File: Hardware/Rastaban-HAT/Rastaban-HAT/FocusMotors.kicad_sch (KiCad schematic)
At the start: 9 parts, among them U6 TMC2208_SILENTSTEPSTICK, U7 DRV8838

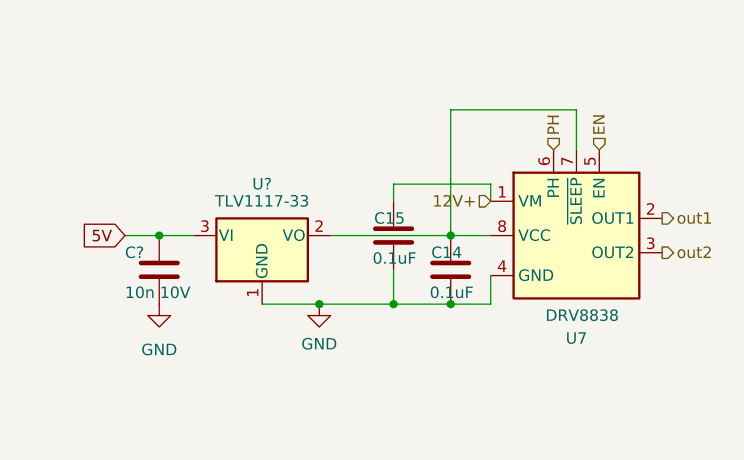
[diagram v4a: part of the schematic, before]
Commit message: updated focus motors and main schematic
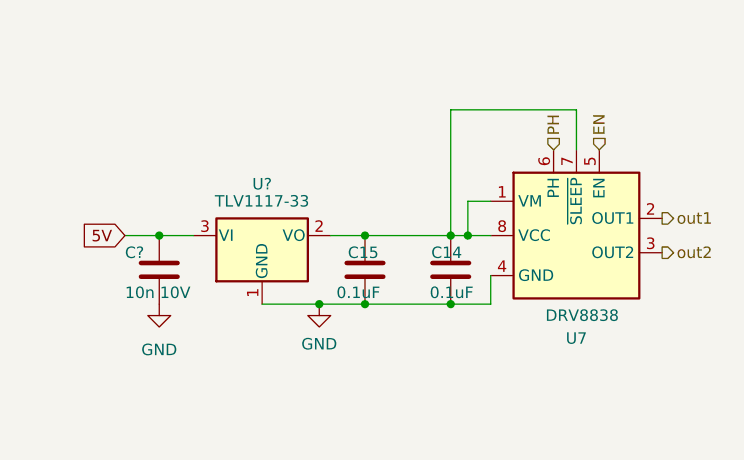
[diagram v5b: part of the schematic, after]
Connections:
- net 12V+: no longer C15.1, U7.1 (VM)
- net GND: now also C15.1; no longer C15.2
- net at C14.1, U7.7 (~{SLEEP}), U7.8 (VCC)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: now also C15.2, U7.1 (VM)
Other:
- moved on the sheet: C15
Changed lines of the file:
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@@
   (junction (at 119.38 122.555) (diameter 0) (color 0 0 0 0)
   )
-  (junction (at 196.215 114.935) (diameter 0) (color 0 0 0 0)
-  )
   (junction (at 202.565 114.935) (diameter 0) (color 0 0 0 0)
   )
+  (junction (at 193.04 107.315) (diameter 0) (color 0 0 0 0)
+  )
   (junction (at 170.18 107.315) (diameter 0) (color 0 0 0 0)
   )
+  (junction (at 204.47 107.315) (diameter 0) (color 0 0 0 0)
+  )
   (junction (at 187.96 114.935) (diameter 0) (color 0 0 0 0)
   )
   (junction (at 73.66 123.825) (diameter 0) (color 0 0 0 0)
+  )
+  (junction (at 193.04 114.935) (diameter 0) (color 0 0 0 0)
   )
   (junction (at 202.565 107.315) (diameter 0) (color 0 0 0 0)
@@
   (no_connect (at 82.55 120.015))
   (no_connect (at 82.55 122.555))
-  (wire (pts (xy 196.215 101.6) (xy 196.215 103.505))
+  (wire (pts (xy 207.01 103.505) (xy 204.47 103.505))
     (stroke (width 0) (type default) (color 0 0 0 0))
   )
@@
     (stroke (width 0) (type default) (color 0 0 0 0))
   )
+  (wire (pts (xy 193.04 107.315) (xy 189.23 107.315))
+    (stroke (width 0) (type default) (color 0 0 0 0))
+  )
   (wire (pts (xy 202.565 114.935) (xy 207.01 114.935))
     (stroke (width 0) (type default) (color 0 0 0 0))
   )
-  (wire (pts (xy 202.565 107.315) (xy 207.01 107.315))
+  (wire (pts (xy 202.565 107.315) (xy 204.47 107.315))
+    (stroke (width 0) (type default) (color 0 0 0 0))
+  )
+  (wire (pts (xy 204.47 107.315) (xy 207.01 107.315))
     (stroke (width 0) (type default) (color 0 0 0 0))
   )
@@
     (stroke (width 0) (type default) (color 0 0 0 0))
   )
-  (wire (pts (xy 207.01 101.6) (xy 196.215 101.6))
-    (stroke (width 0) (type default) (color 0 0 0 0))
-  )
   (wire (pts (xy 82.55 112.395) (xy 69.85 112.395))
     (stroke (width 0) (type default) (color 0 0 0 0))
@@
     (stroke (width 0) (type default) (color 0 0 0 0))
   )
-  (wire (pts (xy 207.01 103.505) (xy 207.01 101.6))
+  (wire (pts (xy 193.04 114.935) (xy 202.565 114.935))
     (stroke (width 0) (type default) (color 0 0 0 0))
   )
@@
     (stroke (width 0) (type default) (color 0 0 0 0))
   )
-  (wire (pts (xy 196.215 111.125) (xy 196.215 114.935))
-    (stroke (width 0) (type default) (color 0 0 0 0))
-  )
   (wire (pts (xy 216.535 97.79) (xy 216.535 93.345))
     (stroke (width 0) (type default) (color 0 0 0 0))
@@
     (stroke (width 0) (type default) (color 0 0 0 0))
   )
-  (wire (pts (xy 202.565 107.315) (xy 189.23 107.315))
+  (wire (pts (xy 193.04 107.315) (xy 202.565 107.315))
     (stroke (width 0) (type default) (color 0 0 0 0))
   )
@@
     (stroke (width 0) (type default) (color 0 0 0 0))
   )
-  (wire (pts (xy 187.96 114.935) (xy 196.215 114.935))
+  (wire (pts (xy 187.96 114.935) (xy 193.04 114.935))
     (stroke (width 0) (type default) (color 0 0 0 0))
   )
@@
     (stroke (width 0) (type default) (color 0 0 0 0))
   )
+  (wire (pts (xy 204.47 103.505) (xy 204.47 107.315))
+    (stroke (width 0) (type default) (color 0 0 0 0))
+  )
   (wire (pts (xy 118.11 97.155) (xy 118.11 100.965))
     (stroke (width 0) (type default) (color 0 0 0 0))
@@
   )
   (wire (pts (xy 119.38 122.555) (xy 118.11 122.555))
-    (stroke (width 0) (type default) (color 0 0 0 0))
-  )
-  (wire (pts (xy 196.215 114.935) (xy 202.565 114.935))
     (stroke (width 0) (type default) (color 0 0 0 0))
   )
@@
   (hierarchical_label "out2" (shape output) (at 226.06 109.22 0)
     (effects (font (size 1.27 1.27)) (justify left))
-  )
-  (hierarchical_label "12V+" (shape input) (at 207.01 103.505 180)
-    (effects (font (size 1.27 1.27)) (justify right))
   )
   (hierarchical_label "3.3V+" (shape input) (at 118.11 97.155 0)
@@
     (pin "VREF")
   )
-  (symbol (lib_id "Device:C") (at 196.215 107.315 0) (unit 1)
+  (symbol (lib_id "Device:C") (at 193.04 111.125 180) (unit 1)
     (in_bom yes) (on_board yes)
-    (property "Reference" "C15" (id 0) (at 197.485 105.41 0)
+    (property "Reference" "C15" (id 0) (at 191.135 109.22 0)
       (effects (font (size 1.27 1.27)) (justify right))
     )
-    (property "Value" "0.1uF" (id 1) (at 198.755 109.855 0)
+    (property "Value" "0.1uF" (id 1) (at 189.865 113.665 0)
       (effects (font (size 1.27 1.27)) (justify right))
     )
-    (property "Footprint" "Capacitor_SMD:C_1206_3216Metric_Pad1.33x1.80mm_HandSolder" (id 2) (at 197.1802 111.125 0)
-      (effects (font (size 1.27 1.27)) hide)
-    )
-    (property "Datasheet" "~" (id 3) (at 196.215 107.315 0)
-      (effects (font (size 1.27 1.27)) hide)
-    )
+    (property "Footprint" "Capacitor_SMD:C_1206_3216Metric_Pad1.33x1.80mm_HandSolder" (id 2) (at 192.0748 107.315 0)
+      (effects (font (size 1.27 1.27)) hide)
+    )
+    (property "Datasheet" "~" (id 3) (at 193.04 111.125 0)
+      (effects (font (size 1.27 1.27)) hide)
+    )

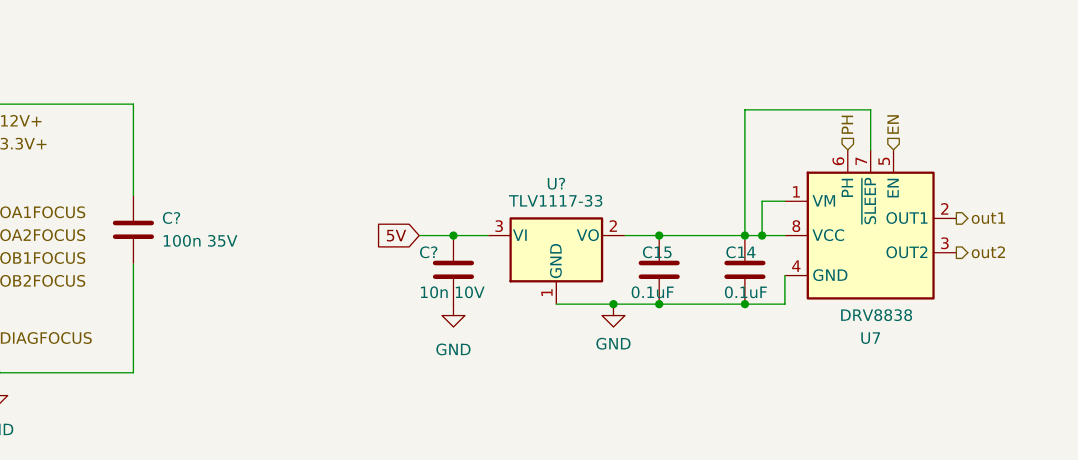
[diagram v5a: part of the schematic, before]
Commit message: added new POLOLU DRV8838 schematic and enh main
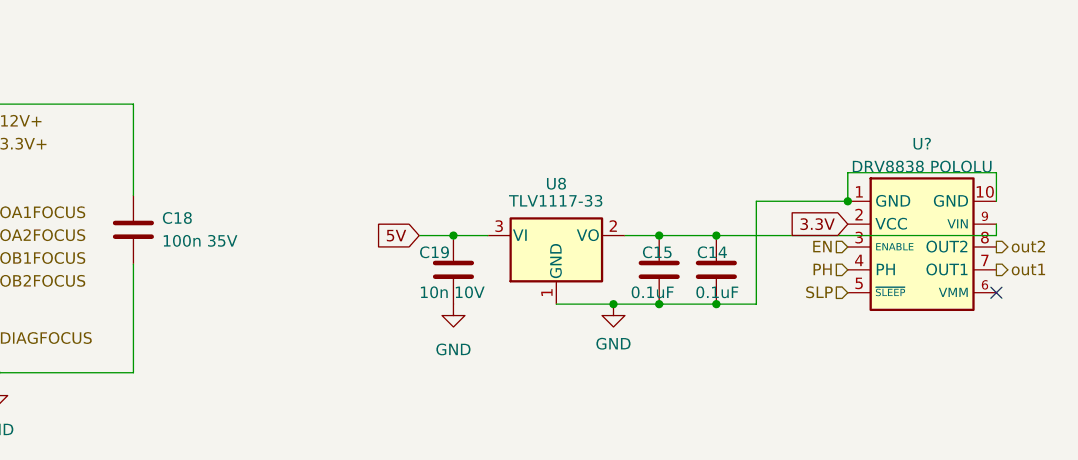
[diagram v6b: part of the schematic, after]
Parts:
- removed U7: DRV8838, Package_SON:WSON-8-1EP_2x2mm_P0.5mm_EP0.9x1.6mm, symbol Driver_Motor:DRV8838
- added U?: DRV8838 POLOLU, Package_SON:WSON-8-1EP_2x2mm_P0.5mm_EP0.9x1.6mm, symbol Driver_Motor:DRV8838 POLOLU
- gave numbers to parts that had none: 3
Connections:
- net EN: now also U?.3 (ENABLE)
- net GND: now also U?.1 (GND), U?.10 (GND)
- net PH: now also U?.4 (PH)
- net out1: now also U?.7 (OUT1)
- net out2: now also U?.8 (OUT2)
- net at C14.1, C15.2, U8.2 (VO): now also U?.9 (VIN)
- new net 3.3V: U?.2 (VCC)
- new net SLP: U?.5 (~{SLEEP})
- no-connect marks 3 -> 4
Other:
- moved on the sheet: C14

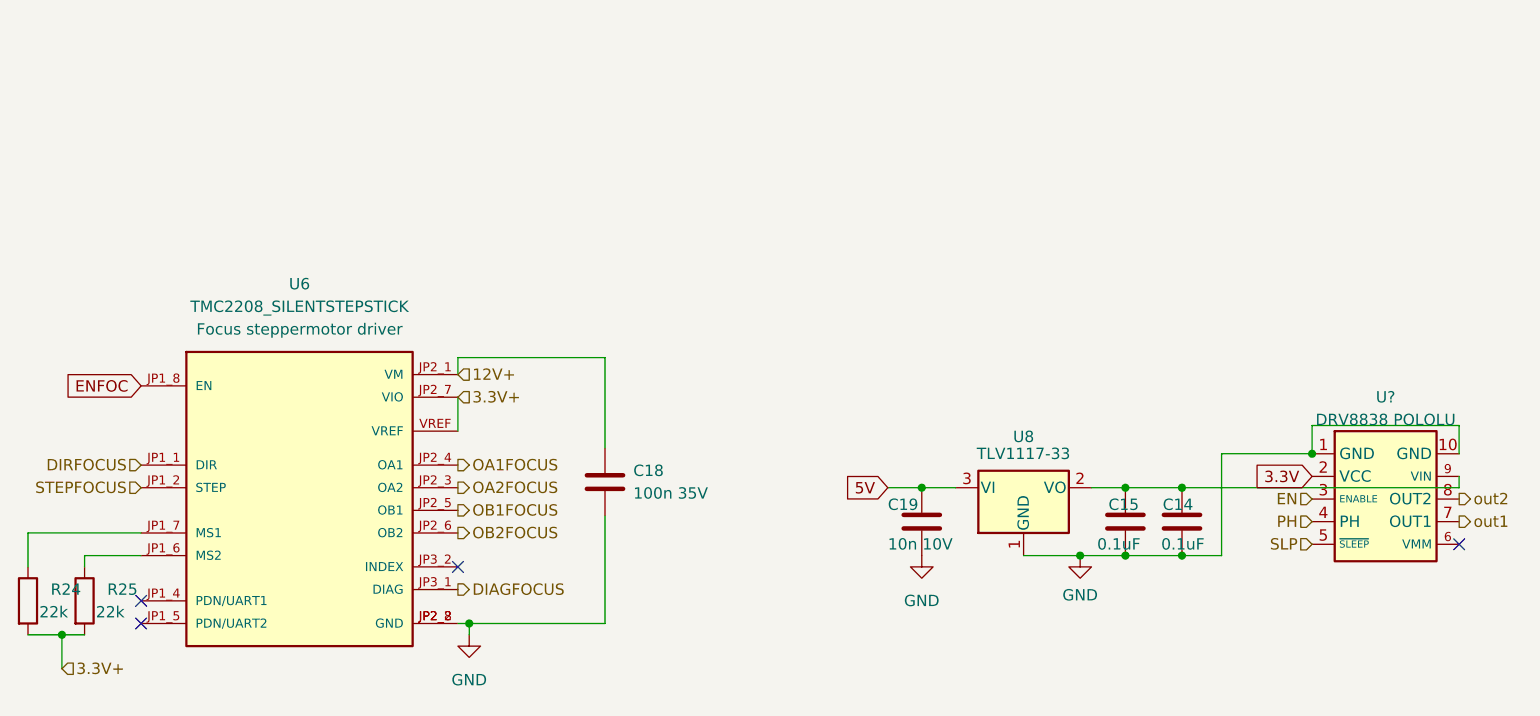
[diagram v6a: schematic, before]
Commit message: updated some names on symbols
stepper motor drivers
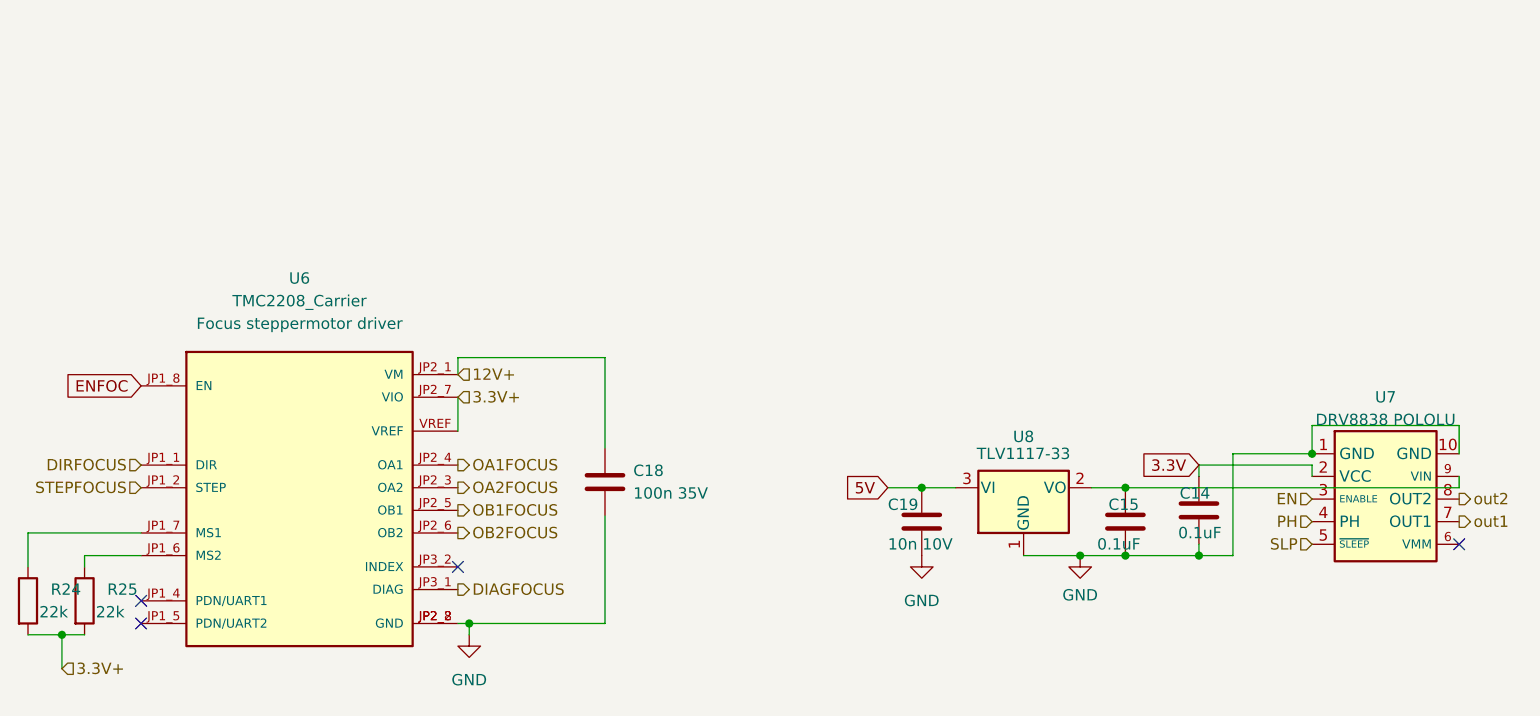
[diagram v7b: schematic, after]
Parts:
- U6: value TMC2208_SILENTSTEPSTICK -> TMC2208_Carrier
- gave numbers to parts that had none: 1
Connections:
- net 3.3V: now also C14.1
- net at C15.2, U7.9 (VIN), U8.2 (VO): no longer C14.1
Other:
- moved on the sheet: C14
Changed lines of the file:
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@@
   (junction (at 213.995 103.505) (diameter 0) (color 0 0 0 0)
   )
-  (junction (at 199.39 107.315) (diameter 0) (color 0 0 0 0)
-  )
-  (junction (at 199.39 114.935) (diameter 0) (color 0 0 0 0)
-  )
   (junction (at 170.18 107.315) (diameter 0) (color 0 0 0 0)
   )
   (junction (at 187.96 114.935) (diameter 0) (color 0 0 0 0)
+  )
+  (junction (at 201.295 114.935) (diameter 0) (color 0 0 0 0)
   )
   (junction (at 73.66 123.825) (diameter 0) (color 0 0 0 0)
@@
     (stroke (width 0) (type default) (color 0 0 0 0))
   )
-  (wire (pts (xy 193.04 114.935) (xy 199.39 114.935))
+  (wire (pts (xy 193.04 114.935) (xy 201.295 114.935))
     (stroke (width 0) (type default) (color 0 0 0 0))
   )
@@
     (stroke (width 0) (type default) (color 0 0 0 0))
   )
-  (wire (pts (xy 199.39 114.935) (xy 203.835 114.935))
-    (stroke (width 0) (type default) (color 0 0 0 0))
-  )
-  (wire (pts (xy 203.835 103.505) (xy 213.995 103.505))
+  (wire (pts (xy 201.295 113.665) (xy 201.295 114.935))
+    (stroke (width 0) (type default) (color 0 0 0 0))
+  )
+  (wire (pts (xy 205.105 103.505) (xy 213.995 103.505))
     (stroke (width 0) (type default) (color 0 0 0 0))
   )
@@
     (stroke (width 0) (type default) (color 0 0 0 0))
   )
+  (wire (pts (xy 201.295 104.775) (xy 213.995 104.775))
+    (stroke (width 0) (type default) (color 0 0 0 0))
+  )
+  (wire (pts (xy 201.295 104.775) (xy 201.295 106.045))
+    (stroke (width 0) (type default) (color 0 0 0 0))
+  )
+  (wire (pts (xy 213.995 104.775) (xy 213.995 106.045))
+    (stroke (width 0) (type default) (color 0 0 0 0))
+  )
   (wire (pts (xy 166.37 107.315) (xy 170.18 107.315))
     (stroke (width 0) (type default) (color 0 0 0 0))
@@
     (stroke (width 0) (type default) (color 0 0 0 0))
   )
-  (wire (pts (xy 203.835 114.935) (xy 203.835 103.505))
+  (wire (pts (xy 205.105 114.935) (xy 205.105 103.505))
     (stroke (width 0) (type default) (color 0 0 0 0))
   )
@@
     (stroke (width 0) (type default) (color 0 0 0 0))
   )
-  (wire (pts (xy 193.04 107.315) (xy 199.39 107.315))
+  (wire (pts (xy 193.04 107.315) (xy 230.505 107.315))
     (stroke (width 0) (type default) (color 0 0 0 0))
   )
@@
     (stroke (width 0) (type default) (color 0 0 0 0))
   )
-  (wire (pts (xy 199.39 107.315) (xy 230.505 107.315))
-    (stroke (width 0) (type default) (color 0 0 0 0))
-  )
   (wire (pts (xy 134.62 92.71) (xy 118.11 92.71))
     (stroke (width 0) (type default) (color 0 0 0 0))
@@
     (stroke (width 0) (type default) (color 0 0 0 0))
   )
-  (global_label "3.3V" (shape input) (at 213.995 106.045 180) (fields_autoplaced)
-    (effects (font (size 1.27 1.27)) (justify right))
-    (property "Intersheet References" "${INTERSHEET_REFS}" (id 0) (at 207.4695 105.9656 0)
+  (wire (pts (xy 201.295 114.935) (xy 205.105 114.935))
+    (stroke (width 0) (type default) (color 0 0 0 0))
+  )
+  (global_label "3.3V" (shape input) (at 201.295 104.775 180) (fields_autoplaced)
+    (effects (font (size 1.27 1.27)) (justify right))
+    (property "Intersheet References" "${INTERSHEET_REFS}" (id 0) (at 194.7695 104.6956 0)
       (effects (font (size 1.27 1.27)) (justify right) hide)
     )
@@
   (symbol (lib_name "TMC2208_SILENTSTEPSTICK_1") (lib_id "TMC2208_SILENTSTEPSTICK:TMC2208_SILENTSTEPSTICK") (at 100.33 109.855 0) (unit 1)
     (in_bom yes) (on_board yes) (fields_autoplaced)
-    (property "Reference" "U6" (id 0) (at 100.33 84.455 0))
-    (property "Value" "TMC2208_SILENTSTEPSTICK" (id 1) (at 100.33 86.995 0))
+    (property "Reference" "U6" (id 0) (at 100.33 83.82 0))
+    (property "Value" "TMC2208_Carrier" (id 1) (at 100.33 86.36 0))
     (property "Footprint" "Footprints:TMC2208_SILENTSTEPSTICK" (id 2) (at 85.09 128.905 0)
       (effects (font (size 1.27 1.27)) (justify left bottom) hide)
@@
       (effects (font (size 1.27 1.27)) (justify left bottom) hide)
     )
-    (property "Purpose" "Focus steppermotor driver" (id 5) (at 100.33 89.535 0))
+    (property "Purpose" "Focus steppermotor driver" (id 5) (at 100.33 88.9 0))
     (pin "JP1_1")
     (pin "JP1_2")
@@
   (symbol (lib_id "Driver_Motor:DRV8838 POLOLU") (at 222.25 106.045 0) (unit 1)
     (in_bom yes) (on_board yes)
-    (property "Reference" "U?" (id 0) (at 222.25 97.155 0))
+    (property "Reference" "U7" (id 0) (at 222.25 97.155 0))
     (property "Value" "DRV8838 POLOLU" (id 1) (at 222.25 99.695 0))
     (property "Footprint" "Package_SON:WSON-8-1EP_2x2mm_P0.5mm_EP0.9x1.6mm" (id 2) (at 226.695 130.81 0)
@@
     (pin "3")
   )
-  (symbol (lib_id "Device:C") (at 199.39 111.125 0) (unit 1)
-    (in_bom yes) (on_board yes)
-    (property "Reference" "C14" (id 0) (at 200.66 109.22 0)
-      (effects (font (size 1.27 1.27)) (justify right))
-    )
-    (property "Value" "0.1uF" (id 1) (at 201.93 113.665 0)
-      (effects (font (size 1.27 1.27)) (justify right))
-    )
-    (property "Footprint" "Capacitor_SMD:C_1206_3216Metric_Pad1.33x1.80mm_HandSolder" (id 2) (at 200.3552 114.935 0)
-      (effects (font (size 1.27 1.27)) hide)
-    )
-    (property "Datasheet" "~" (id 3) (at 199.39 111.125 0)
-      (effects (font (size 1.27 1.27)) hide)
-    )
+  (symbol (lib_id "Device:C") (at 201.295 109.855 0) (unit 1)
+    (in_bom yes) (on_board yes)
+    (property "Reference" "C14" (id 0) (at 202.565 107.95 0)
+      (effects (font (size 1.27 1.27)) (justify right))
+    )
+    (property "Value" "0.1uF" (id 1) (at 203.835 112.395 0)
+      (effects (font (size 1.27 1.27)) (justify right))
+    )
+    (property "Footprint" "Capacitor_SMD:C_1206_3216Metric_Pad1.33x1.80mm_HandSolder" (id 2) (at 202.2602 113.665 0)
+      (effects (font (size 1.27 1.27)) hide)
+    )
+    (property "Datasheet" "~" (id 3) (at 201.295 109.855 0)
+      (effects (font (size 1.27 1.27)) hide)
+    )

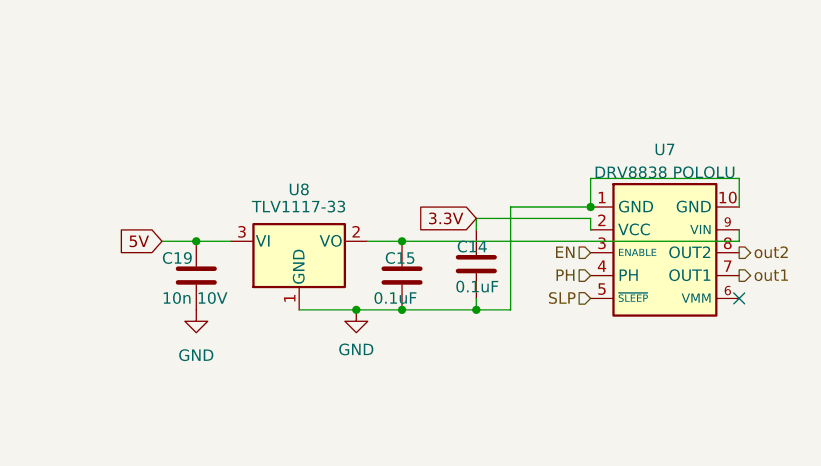
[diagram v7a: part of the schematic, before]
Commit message: changed revision to v1.1 on all tabs
changed some capacitor values
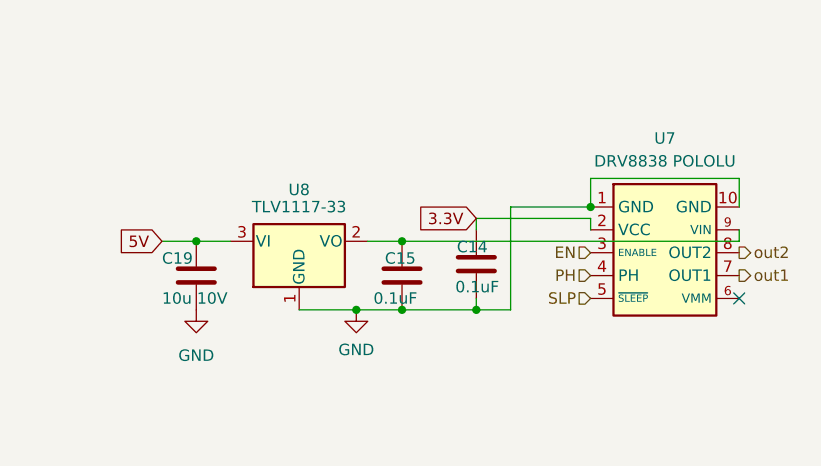
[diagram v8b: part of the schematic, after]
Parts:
- C19: value 10n 10V -> 10u 10V
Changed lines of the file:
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@@
   (title_block
     (title "Rastaban-HAT")
-    (rev "1")
+    (rev "1.1")
     (company "HAN")
     (comment 1 "Casper R. Tak")
@@
   (symbol (lib_id "Driver_Motor:DRV8838 POLOLU") (at 222.25 106.045 0) (unit 1)
     (in_bom yes) (on_board yes)
-    (property "Reference" "U7" (id 0) (at 222.25 97.155 0))
-    (property "Value" "DRV8838 POLOLU" (id 1) (at 222.25 99.695 0))
+    (property "Reference" "U7" (id 0) (at 222.25 95.885 0))
+    (property "Value" "DRV8838 POLOLU" (id 1) (at 222.25 98.425 0))
     (property "Footprint" "Package_SON:WSON-8-1EP_2x2mm_P0.5mm_EP0.9x1.6mm" (id 2) (at 226.695 130.81 0)
       (effects (font (size 1.27 1.27)) hide)
@@
       (effects (font (size 1.27 1.27)) (justify left))
     )
-    (property "Value" "10n 10V" (id 1) (at 166.37 113.665 0)
-      (effects (font (size 1.27 1.27)) (justify left))
-    )
+    (property "Value" "10u 10V" (id 1) (at 166.37 113.665 0)
+      (effects (font (size 1.27 1.27)) (justify left))
+    )
